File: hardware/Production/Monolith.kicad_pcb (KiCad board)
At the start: 6 copper layers, 43.2 x 74.4 mm, 307 parts, among them J102 Cell 1 NTC wires, J105 Cell 2 NTC wires, J106 Cell 3 NTC wires, J107 Cell 4 NTC wires, J108 PACK- power wire, J109 CELL1 sense wire, J110 CELL2 sense wire, J111 CELL3 sense wire, J112 PACK+ power wire, J113 LOAD PACK_P, J114 LOAD GND, J115 1N Kelvin wire, J116 4P Kelvin wire, J301 TC2030-NL, J302 TC2030-NL GAUGE, J401 TYPE-C 16PCB1.6 IP68, J501 TYPE-C 16PCB1.6 IP68, Q101 BSC007N04LS6, Q102 BSC007N04LS6, Q103 AO3400A, Q104 AO3400A, Q401 SiZ240DT, Q402 SiZ240DT, Q409 AO3400A, Q501 SiZ240DT, Q502 SiZ240DT, Q509 AO3400A, U101 BQ40Z50RSMR-R2, U102 BQ294700DSGR, U204 TPS62177DQCR, U301 CC2340R5MODA, U401 TPS25751DREFR, U402 M24512-DFMC6TG, U403 BQ25756RRVR, U404 TPS62933DRLR, U405 TPD6S300RUKR, U406 TPS7A4101DGNR, U501 TPS25751DREFR, U502 M24512-DFMC6TG, U503 BQ25756RRVR, U504 TPS62933DRLR, U505 TPD6S300RUKR, U506 TPS7A4101DGNR

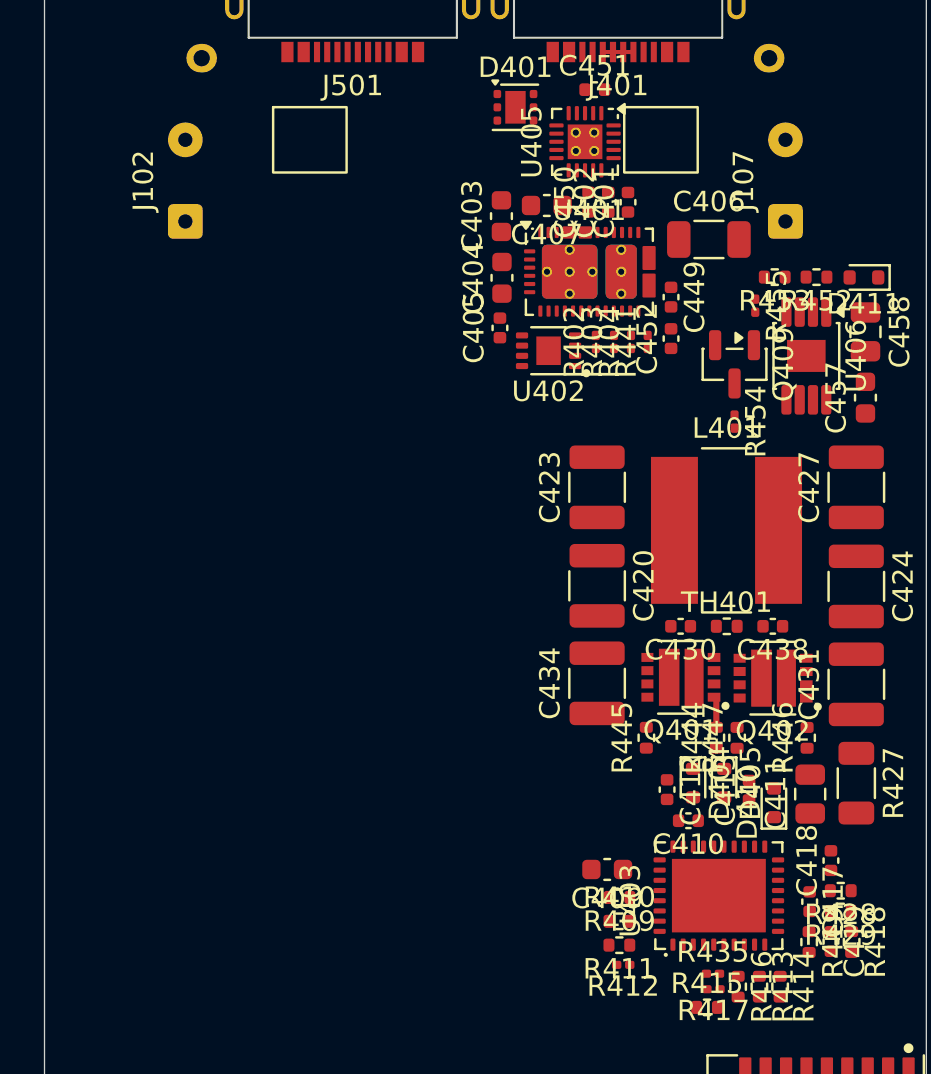
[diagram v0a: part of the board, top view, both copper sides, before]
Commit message: Front-cell NTCs: SMD on the board (TH101 / TH104) instead of wired beads
TS1 / TS4 move from wired beads on the cans (J102 / J107) to 0402 NTCs
(NCP15XH103F03RC) on B.Cu in the outer bottom corner of each gap-filler
zone, |y| 15.5 mm, z 29 mm, outboard of port 1's BQ25756. In the 3-D model
with the 10-27 stage layout they read 0.6-3.8 K above the hottest can point
and never below it. The discharge ramp moves up 2 K (44 -> 48 C) to keep
the same energy; charge ramp and gauge limits unchanged.

- gauge.kicad_sch: J102 / J107 -> TH101 / TH104, sheet note 4
- Monolith.kicad_pcb: TH101 / TH104 placed and locked on B.Cu, J102 / J107
  and KO_B_ntc_* removed, KO_B_gap_filler_L/_R notched for the parts
- monolith_shell sb_ntc_smd(), make_board / make_production follow it
- spec, firmware policy, assembly, bring-up, board README, step 2 render
- smd.py: p0b layout, spot probes and policy runs; smd-ntc.md rewritten

Co-Authored-By: Claude Opus 5.5 <noreply@anthropic.com>
Claude-Session: https://claude.ai/code/session_01LzE9uxopd3CrLAEeFamvpR
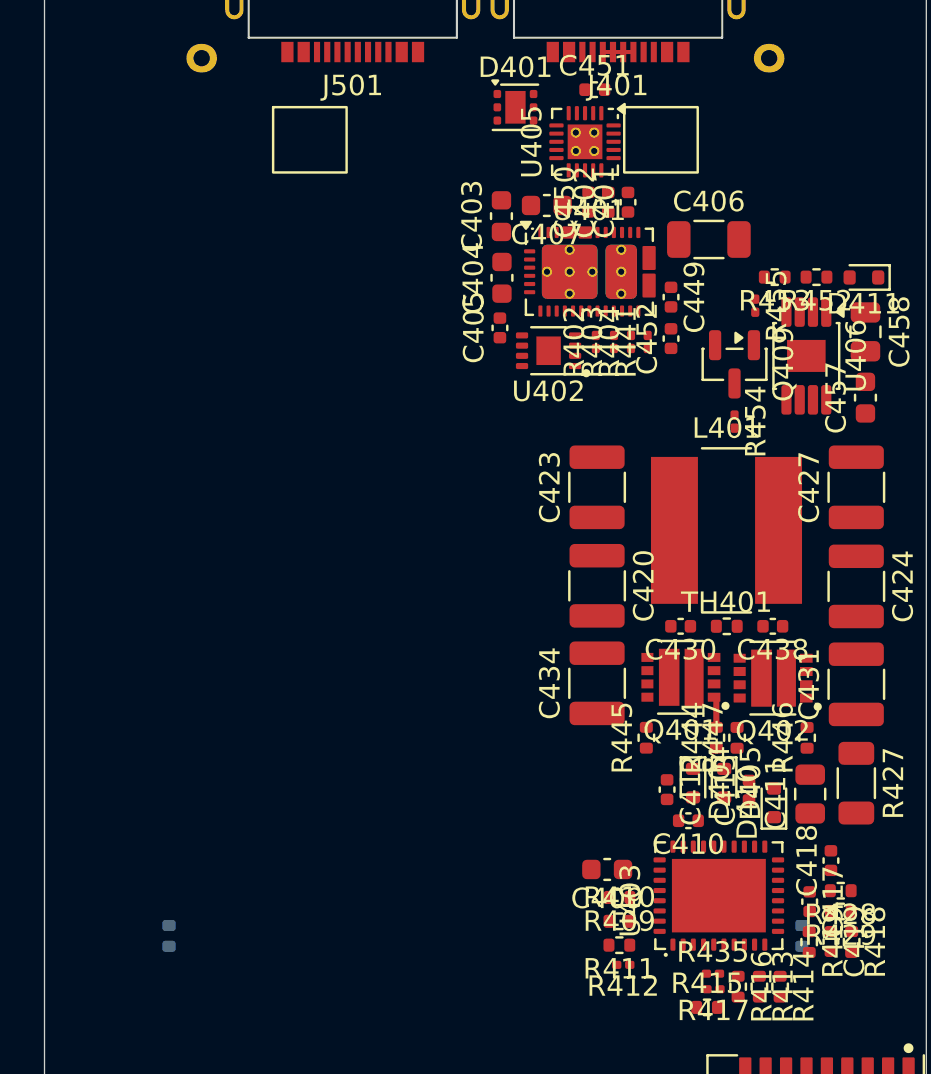
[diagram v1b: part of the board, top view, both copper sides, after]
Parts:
- removed J102: Cell 1 NTC wires, Connector_Wire:SolderWire-0.15sqmm_1x02_P4mm_D0.5mm_OD1.5mm
- removed J107: Cell 4 NTC wires, Connector_Wire:SolderWire-0.15sqmm_1x02_P4mm_D0.5mm_OD1.5mm
- added TH101: 10k B3435, Resistor_SMD:R_0402_1005Metric, B.Cu at (84.5, 112.5)
- added TH104: 10k B3435, Resistor_SMD:R_0402_1005Metric, B.Cu at (115.5, 112.5)
